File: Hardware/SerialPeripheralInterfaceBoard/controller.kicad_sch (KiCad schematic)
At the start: 5 parts, among them U1 74HC238, U12 74HC00, U2 74HC74, U3 74HC02, U4 74HC04

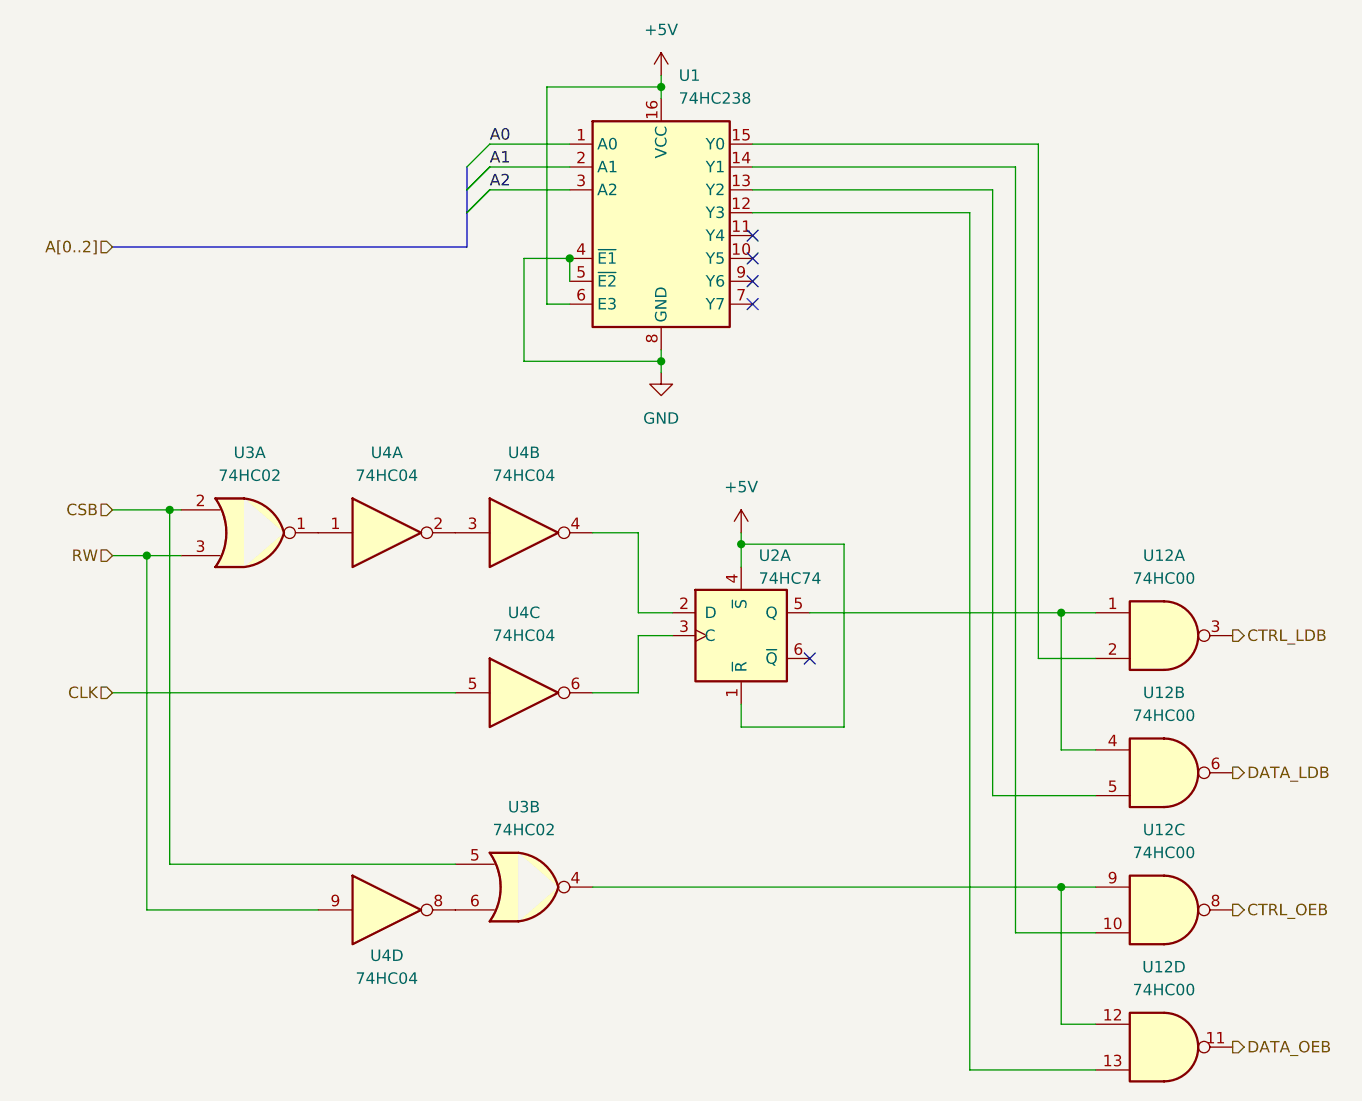
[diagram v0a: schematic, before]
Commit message: feat: modify mother board for paging and dma
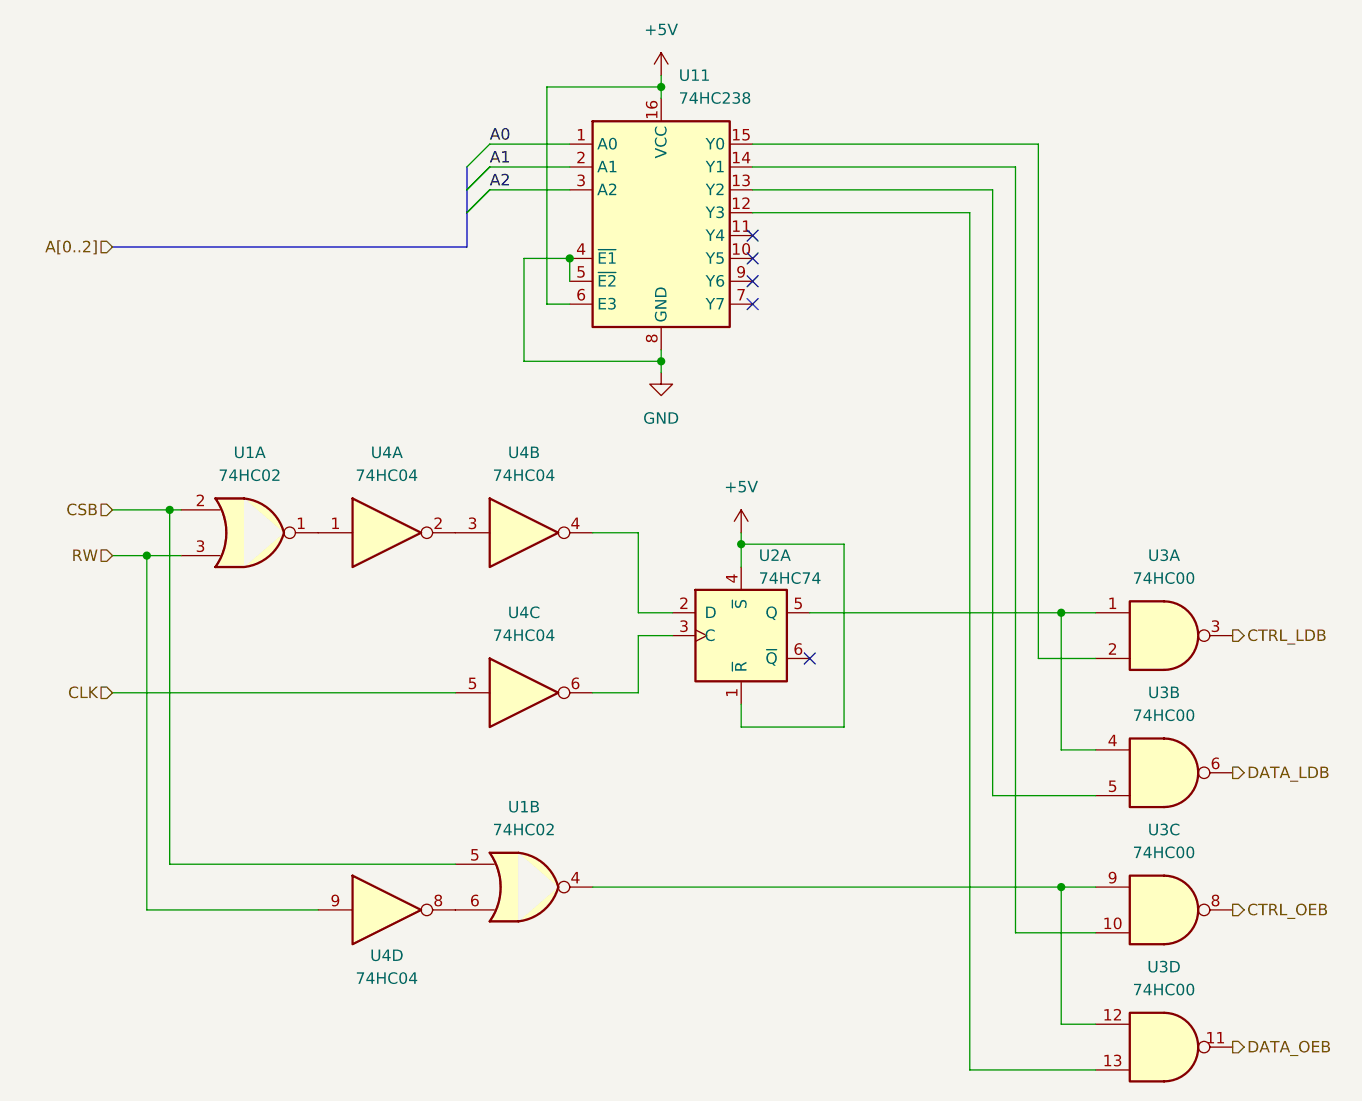
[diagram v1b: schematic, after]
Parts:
- renumbered U3 to U1, U1 to U11, U12 to U3
